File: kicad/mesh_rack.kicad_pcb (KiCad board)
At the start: 4 copper layers, 200 x 100 mm, 20 parts, among them IC1 E22-900M22S, J1 Input, U1 INA260, U2 ESP32-S3-WROOM-1, U3 LM22678TJ-5, U4 LM2596S-3.3, U5 TPD2EUSB30

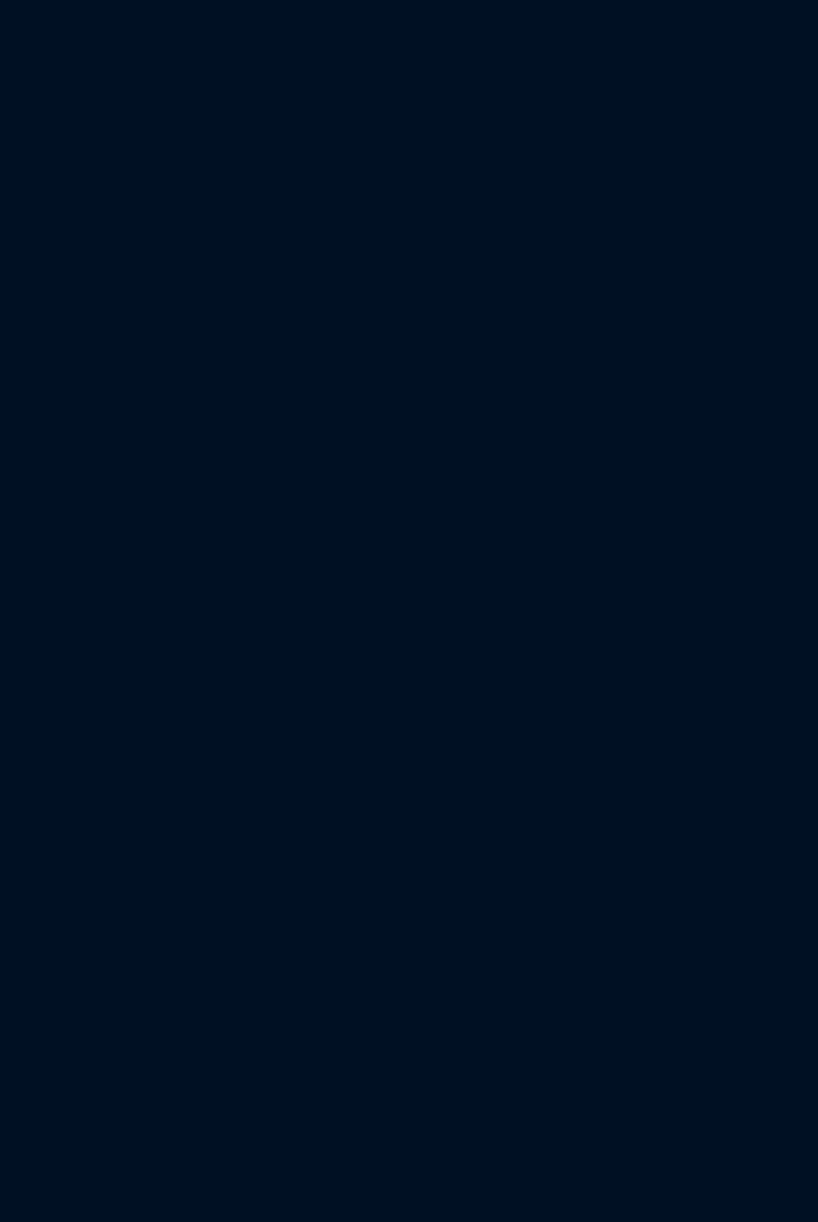
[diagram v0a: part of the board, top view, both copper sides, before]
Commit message: add expansin headers
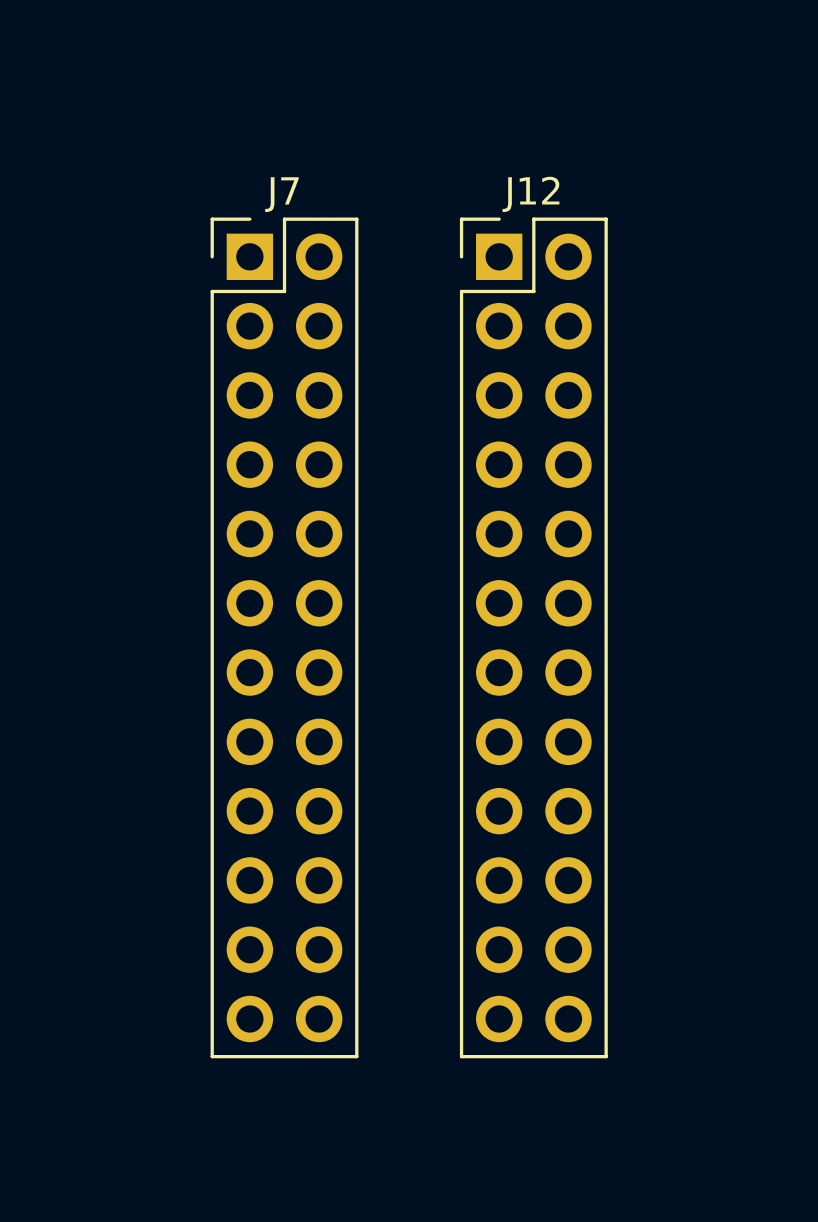
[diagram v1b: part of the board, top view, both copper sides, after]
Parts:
- added J12: Conn_02x12_Odd_Even, Connector_PinHeader_2.54mm:PinHeader_2x12_P2.54mm_Vertical, F.Cu at (250.7, 49.1)
- added J7: Conn_02x12_Odd_Even, Connector_PinHeader_2.54mm:PinHeader_2x12_P2.54mm_Vertical, F.Cu at (241.6, 49.1)

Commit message: finish pcb
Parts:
- removed J12: Conn_02x12_Odd_Even, Connector_PinHeader_2.54mm:PinHeader_2x12_P2.54mm_Vertical
- removed JP1: A0, Jumper:SolderJumper-2_P1.3mm_Open_TrianglePad1.0x1.5mm
- removed JP2: A1, Jumper:SolderJumper-2_P1.3mm_Open_TrianglePad1.0x1.5mm
- added C1: 10uF, Capacitor_SMD:C_0805_2012Metric, F.Cu at (114.2, 33.2)
- added C10: 47uF, Capacitor_SMD:C_0805_2012Metric, F.Cu at (71.2, 80.8)
- added C11: 100nF, Capacitor_SMD:C_0805_2012Metric, F.Cu at (59.0, 83.8)
- added C12: 100nF, Capacitor_SMD:C_0805_2012Metric, F.Cu at (69.2, 100.2)
- added C13: 0.1uF, Capacitor_SMD:C_0805_2012Metric, F.Cu at (99.5, 86.9)
- added C14: 470uF, Capacitor_SMD:C_0805_2012Metric, F.Cu at (76.8, 92.9)
- added C15: 10uF, Capacitor_SMD:C_0805_2012Metric, F.Cu at (78.8, 92.9)
- added C16: 0.1uF, Capacitor_SMD:C_0805_2012Metric, F.Cu at (80.8, 92.9)
- added C17: 470uF, Capacitor_SMD:C_0805_2012Metric, F.Cu at (82.8, 92.9)
- added C18: 22uF, Capacitor_SMD:C_0805_2012Metric, F.Cu at (99.5, 80.9)
- added C19: 680uF, Capacitor_SMD:C_0805_2012Metric, F.Cu at (99.5, 82.9)
- added C2: 0.1uF, Capacitor_SMD:C_0805_2012Metric, F.Cu at (112.2, 33.2)
- added C20: 680uF, Capacitor_SMD:C_0805_2012Metric, F.Cu at (99.5, 84.9)
- added C21: 0.1uF, Capacitor_SMD:C_0805_2012Metric, F.Cu at (74.8, 101.4)
- added C22: 100nF, Capacitor_SMD:C_0805_2012Metric, F.Cu at (189.1, 35.0)
- added C23: 10uF, Capacitor_SMD:C_0805_2012Metric, F.Cu at (189.1, 33.0)
- added C24: 0.1uF, Capacitor_SMD:C_0805_2012Metric, F.Cu at (111.5, 41.8)
- added C3: 1uF, Capacitor_SMD:C_0805_2012Metric, F.Cu at (106.2, 39.0)
- added C4: 0.1uF, Capacitor_SMD:C_0805_2012Metric, F.Cu at (155.6, 47.7)
- added C5: 22uF, Capacitor_SMD:C_0805_2012Metric, F.Cu at (45.8, 83.2)
- added C6: 22uF, Capacitor_SMD:C_0805_2012Metric, F.Cu at (48.8, 83.2)
- added C7: 100uF, Capacitor_SMD:C_0805_2012Metric, F.Cu at (51.8, 83.2)
- added C8: 47uF, Capacitor_SMD:C_0805_2012Metric, F.Cu at (71.2, 74.7)
- added C9: 220uF, Capacitor_SMD:C_0805_2012Metric, F.Cu at (71.2, 77.8)
- added D4: LED, LED_THT:LED_D5.0mm, F.Cu at (130.8, 60.0)
- added D5: LED, LED_THT:LED_D5.0mm, F.Cu at (48.2, 30.2)
- added D6: LED, LED_THT:LED_D5.0mm, F.Cu at (106.8, 91.2)
- added D7: LED, LED_THT:LED_D5.0mm, F.Cu at (77.8, 73.7)
- added D8: LED, LED_THT:LED_D5.0mm, F.Cu at (65.5, 110.2)
- added D9: LED, LED_THT:LED_D5.0mm, F.Cu at (124.2, 60.0)
- added J10: Conn_01x02, Connector_PinSocket_2.54mm:PinSocket_1x02_P2.54mm_Vertical, F.Cu at (41.0, 43.8)
- added J11: Conn_01x04, Connector_PinHeader_2.54mm:PinHeader_1x04_P2.54mm_Vertical, F.Cu at (99.0, 51.1)
- added J2: Power Switch, TerminalBlock_Altech:Altech_AK100_1x02_P5.00mm, F.Cu at (44.1, 95.0)
- added J3: USB_C_Receptacle_USB2.0_14P, Connector_USB:USB_C_Receptacle_HRO_TYPE-C-31-M-12, F.Cu at (82.5, 29.7)
- added J4: Conn_01x02, Connector_PinSocket_2.54mm:PinSocket_1x02_P2.54mm_Vertical, F.Cu at (61.0, 44.8)
- added J5: BOOT, Connector_PinHeader_2.54mm:PinHeader_1x02_P2.54mm_Vertical, F.Cu at (151.0, 46.5)
- added J6: EN, Connector_PinHeader_2.54mm:PinHeader_1x02_P2.54mm_Vertical, F.Cu at (105.2, 42.0)
- added J8: Conn_02x09_Counter_Clockwise, Connector_PinHeader_2.54mm:PinHeader_2x09_P2.54mm_Vertical, F.Cu at (178.4, 80.5)
- added J9: Conn_01x10, Connector_PinSocket_2.54mm:PinSocket_1x10_P2.54mm_Vertical, F.Cu at (146.5, 79.6)
- added L1: 10uH Coilcraft XAL7030-103, Inductor_SMD:L_Coilcraft_XAL7030-103, F.Cu at (64.8, 77.8)
- added L2: 22uH, Inductor_SMD:L_12x12mm_H4.5mm, F.Cu at (86.5, 83.9)
- added Q1: IRF9540N, Package_TO_SOT_THT:TO-220-3_Vertical, F.Cu at (44.2, 106.5)
- added Q2: IRF540N, Package_TO_SOT_THT:TO-220-3_Vertical, F.Cu at (53.5, 54.2)
- added R1: 10k, Resistor_THT:R_Axial_DIN0207_L6.3mm_D2.5mm_P10.16mm_Horizontal, F.Cu at (102.4, 36.5)
- added R10: 47k, Resistor_THT:R_Axial_DIN0207_L6.3mm_D2.5mm_P10.16mm_Horizontal, F.Cu at (74.7, 105.9)
- added R11: 47k, Resistor_THT:R_Axial_DIN0207_L6.3mm_D2.5mm_P10.16mm_Horizontal, F.Cu at (98.4, 105.9)
- added R12: 22, Resistor_SMD:R_0805_2012Metric_Pad1.20x1.40mm_HandSolder, F.Cu at (83.2, 39.2)
- added R13: 22, Resistor_SMD:R_0805_2012Metric_Pad1.20x1.40mm_HandSolder, F.Cu at (81.2, 39.2)
- added R14: 5.1k, Resistor_SMD:R_0805_2012Metric_Pad1.20x1.40mm_HandSolder, F.Cu at (77.8, 39.2)
- added R15: 5.1k, Resistor_SMD:R_0805_2012Metric_Pad1.20x1.40mm_HandSolder, F.Cu at (86.8, 39.2)
- added R16: 10k, Resistor_THT:R_Axial_DIN0207_L6.3mm_D2.5mm_P10.16mm_Horizontal, F.Cu at (150.4, 59.2)
- added R17: 10k, Resistor_THT:R_Axial_DIN0207_L6.3mm_D2.5mm_P10.16mm_Horizontal, F.Cu at (160.3, 77.0)
- added R18: 10k, Resistor_THT:R_Axial_DIN0207_L6.3mm_D2.5mm_P10.16mm_Horizontal, F.Cu at (150.6, 53.4)
- added R19: 10k, Resistor_THT:R_Axial_DIN0207_L6.3mm_D2.5mm_P10.16mm_Horizontal, F.Cu at (142.8, 53.8)
- added R2: 10k, Resistor_THT:R_Axial_DIN0207_L6.3mm_D2.5mm_P10.16mm_Horizontal, F.Cu at (68.0, 28.9)
- added R20: 10k, Resistor_THT:R_Axial_DIN0207_L6.3mm_D2.5mm_P10.16mm_Horizontal, F.Cu at (117.0, 64.1)
- added R21: 10k, Resistor_THT:R_Axial_DIN0207_L6.3mm_D2.5mm_P10.16mm_Horizontal, F.Cu at (71.0, 114.8)
- added R22: 10k, Resistor_THT:R_Axial_DIN0207_L6.3mm_D2.5mm_P10.16mm_Horizontal, F.Cu at (124.5, 64.2)
- added R3: 10k, Resistor_THT:R_Axial_DIN0207_L6.3mm_D2.5mm_P10.16mm_Horizontal, F.Cu at (130.8, 64.2)
- added R4: 10k, Resistor_THT:R_Axial_DIN0207_L6.3mm_D2.5mm_P10.16mm_Horizontal, F.Cu at (48.9, 108.8)
- added R5: 10k, Resistor_THT:R_Axial_DIN0207_L6.3mm_D2.5mm_P10.16mm_Horizontal, F.Cu at (51.7, 30.5)
- added R6: 10k, Resistor_THT:R_Axial_DIN0207_L6.3mm_D2.5mm_P10.16mm_Horizontal, F.Cu at (111.0, 91.4)
- added R7: 10k, Resistor_THT:R_Axial_DIN0207_L6.3mm_D2.5mm_P10.16mm_Horizontal, F.Cu at (81.4, 73.8)
- added R8: 100k, Resistor_THT:R_Axial_DIN0207_L6.3mm_D2.5mm_P10.16mm_Horizontal, F.Cu at (63.6, 103.2)
- added R9: 18k, Resistor_THT:R_Axial_DIN0207_L6.3mm_D2.5mm_P10.16mm_Horizontal, F.Cu at (53.4, 100.2)
- J7: value Conn_02x12_Odd_Even -> Conn_Coaxial_Small; footprint Connector_PinHeader_2.54mm:PinHeader_2x12_P2.54mm_Vertical -> Connector_Coaxial:U.FL_Molex_MCRF_73412-0110_Vertical
- U1: value INA260 -> NEO-M8N; footprint Package_SO:TSSOP-16_4.4x5mm_P0.65mm -> RF_GPS:ublox_NEO
- moved U1 225.7 mm to (51.0, 43.2)
- moved U5 211.8 mm to (82.2, 43.4)
- moved J1 204.9 mm to (48.8, 112.8)
- moved J7 203.3 mm to (38.2, 49.0), turned to 90 degrees
- moved D1 198.1 mm to (49.0, 104.2), turned to -90 degrees
- moved D2 187.0 mm to (76.3, 86.1), turned to 90 degrees
- moved U3 181.8 mm to (62.9, 91.5)
- moved D3 179.7 mm to (58.0, 115.2), turned to -90 degrees
- moved U4 152.6 mm to (95.2, 98.0)
- moved U2 148.7 mm to (125.1, 38.0)
- moved IC1 120.6 mm to (195.8, 45.0), turned to 90 degrees
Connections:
- IC1 pad 13: /ESP32/IO7 -> /ESP32/LORA_DIO1
- IC1 pad 14: /LoRa/IO0 -> /ESP32/LORA_BUSY
- IC1 pad 15: /LoRa/IO1 -> /ESP32/LORA_RST
- IC1 pad 16: /ESP32/IO10 -> /ESP32/LORA_MISO
- IC1 pad 17: /ESP32/IO11 -> /ESP32/LORA_MOSI
- IC1 pad 18: /ESP32/IO18 -> /ESP32/LORA_SCK
- IC1 pad 19: /ESP32/IO16 -> /ESP32/LORA_NSS
- IC1 pad 6: /LoRa/IO2 -> /ESP32/LORA_RF_SW
- IC1 pad 7: /ESP32/IO9 -> Net-(IC1-DIO2)
- IC1 pad 8: /ESP32/IO8 -> Net-(IC1-DIO2)
- J7 pad 1: Net-(J7-Pin_1) -> Net-(J7-In)
- J7 pad 2: Net-(J7-Pin_1) -> GND
- U1 pad 1: Net-(J2-Pin_2) -> unconnected-(U1-~{SAFEBOOT}-Pad1)
- U1 pad 10: +3.3V -> Net-(Q2-D)
- U1 pad 11: GND -> Net-(J7-In)
- U1 pad 12: Net-(J2-Pin_2) -> Net-(Q2-D)
- U1 pad 13: unconnected-(U1-NC-Pad13) -> Net-(Q2-D)
- U1 pad 14: /Power Input/RAW -> unconnected-(U1-LNA_EN-Pad14)
- U1 pad 15: /Power Input/RAW -> unconnected-(U1-RESERVED-Pad15)
- U1 pad 16: /Power Input/RAW -> unconnected-(U1-RESERVED-Pad16)
- U1 pad 2: Net-(J2-Pin_2) -> unconnected-(U1-D_SEL-Pad2)
- U1 pad 3: Net-(J2-Pin_2) -> /GPS/TIMEPULSE
- U1 pad 4: Net-(JP2-B) -> unconnected-(U1-EXTINT-Pad4)
- U1 pad 5: Net-(JP1-B) -> /GPS/GPS_USB_D-
- U1 pad 6: GND -> /GPS/GPS_USB_D+
- U1 pad 7: /ESP32/IO4 -> GND
- U1 pad 8: /ESP32/IO5 -> /ESP32/IO47
- U1 pad 9: /ESP32/IO6 -> unconnected-(U1-VCC_RF-Pad9)
- U2 pad 10: /ESP32/IO17 -> /ESP32/OLED_SDA
- U2 pad 11: /ESP32/IO18 -> /ESP32/OLED_SCL
- U2 pad 12: /ESP32/IO8 -> /ESP32/LORA_SCK
- U2 pad 17: /ESP32/IO9 -> /ESP32/LORA_MISO
- U2 pad 18: /ESP32/IO10 -> /ESP32/LORA_MOSI
- U2 pad 23: /ESP32/IO21 -> /ESP32/TST_PD0
- U2 pad 25: /ESP32/IO48 -> /ESP32/LED
- U2 pad 31: /ESP32/IO38 -> /ESP32/LORA_RF_SW
- U2 pad 32: /ESP32/IO39 -> /ESP32/LORA_DIO1
- U2 pad 33: /ESP32/IO40 -> /ESP32/LORA_BUSY
- U2 pad 34: /ESP32/IO41 -> /ESP32/LORA_NSS
- U2 pad 35: /ESP32/IO42 -> /ESP32/LORA_RST
- U2 pad 36: /ESP32/RXD0 -> /ESP32/MCU_RXD0
- U2 pad 37: /ESP32/TXD0 -> /ESP32/MCU_TXD0
- U2 pad 39: /ESP32/IO1 -> /ESP32/ADC1
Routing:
- net +5V: track 0.00 -> 196.8 mm
- net +3.3V: track 0.00 -> 172.6 mm, vias 0 -> 1
- net GND: track 0.00 -> 150.7 mm, vias 0 -> 356
- net /ESP32/IO47: track 0.00 -> 114.0 mm, vias 0 -> 1
- net /ESP32/IO16: track 0.00 -> 110.0 mm, vias 0 -> 2
- net /ESP32/IO45: track 0.00 -> 109.6 mm
- net /ESP32/IO5: track 0.00 -> 100.7 mm, vias 0 -> 1
- net /ESP32/IO7: track 0.00 -> 99.5 mm, vias 0 -> 1
- net /ESP32/LORA_SCK: track 0.00 -> 90.7 mm, vias 0 -> 2
- net /ESP32/IO11: track 0.00 -> 90.1 mm, vias 0 -> 1
- net /ESP32/IO6: track 0.00 -> 88.8 mm, vias 0 -> 1
- net /ESP32/LORA_MISO: track 0.00 -> 86.7 mm, vias 0 -> 2
- net /ESP32/IO46: track 0.00 -> 85.9 mm
- net /ESP32/MCU_RXD0: track 0.00 -> 83.0 mm, vias 0 -> 2
- net /ESP32/MCU_TXD0: track 0.00 -> 82.8 mm, vias 0 -> 2
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- added copper zone on In2.Cu, net +3.3V
- added copper zone on F.Cu, net +5V
- added copper zone on F.Cu, net GND
- added copper zone on F.Cu, net Net-(Q2-D)
- added copper zone on F.Cu, net Net-(U3-SW)
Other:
- board text added: "ADC1 IO3 IO5 IO7 IO16 5V 3.3V 3.3V GND"
- board text added: "BOOT"
- board text added: "D+"
- board text added: "D-"
- board text added: "DAT2 DAT3 CD CMD VDD CLK VSS DAT0 DAT1 DET SHIELD"
- board text added: "EN"
- board text added: "IO2 IO4 IO6 IO11 IO46 5V 3.3V GND GND"
- board text added: "SCL"
- board text added: "SDA"
- board text added: "SDA SCL 3.3V GND"

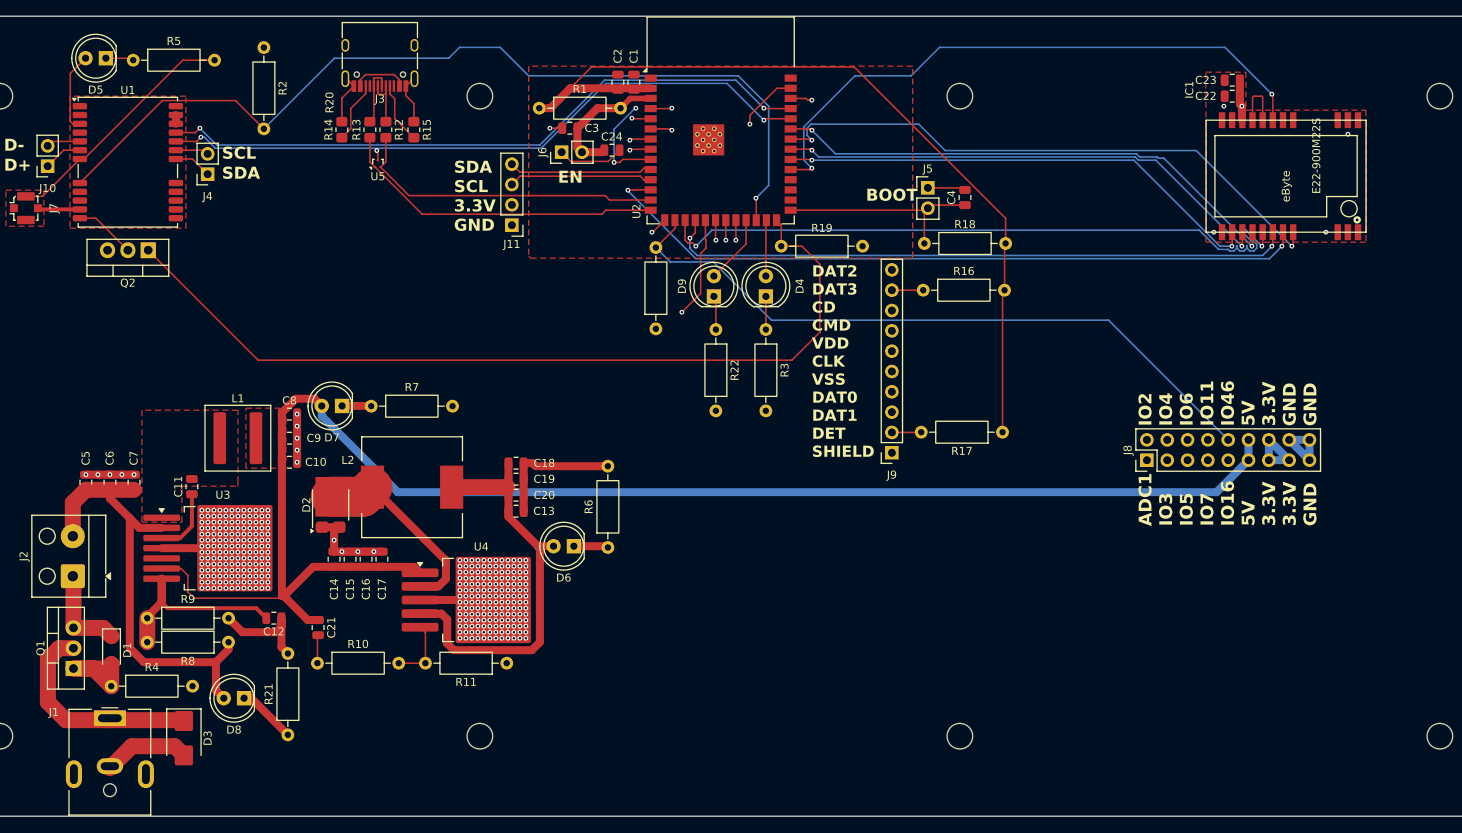
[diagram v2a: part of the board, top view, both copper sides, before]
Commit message: add current sensor
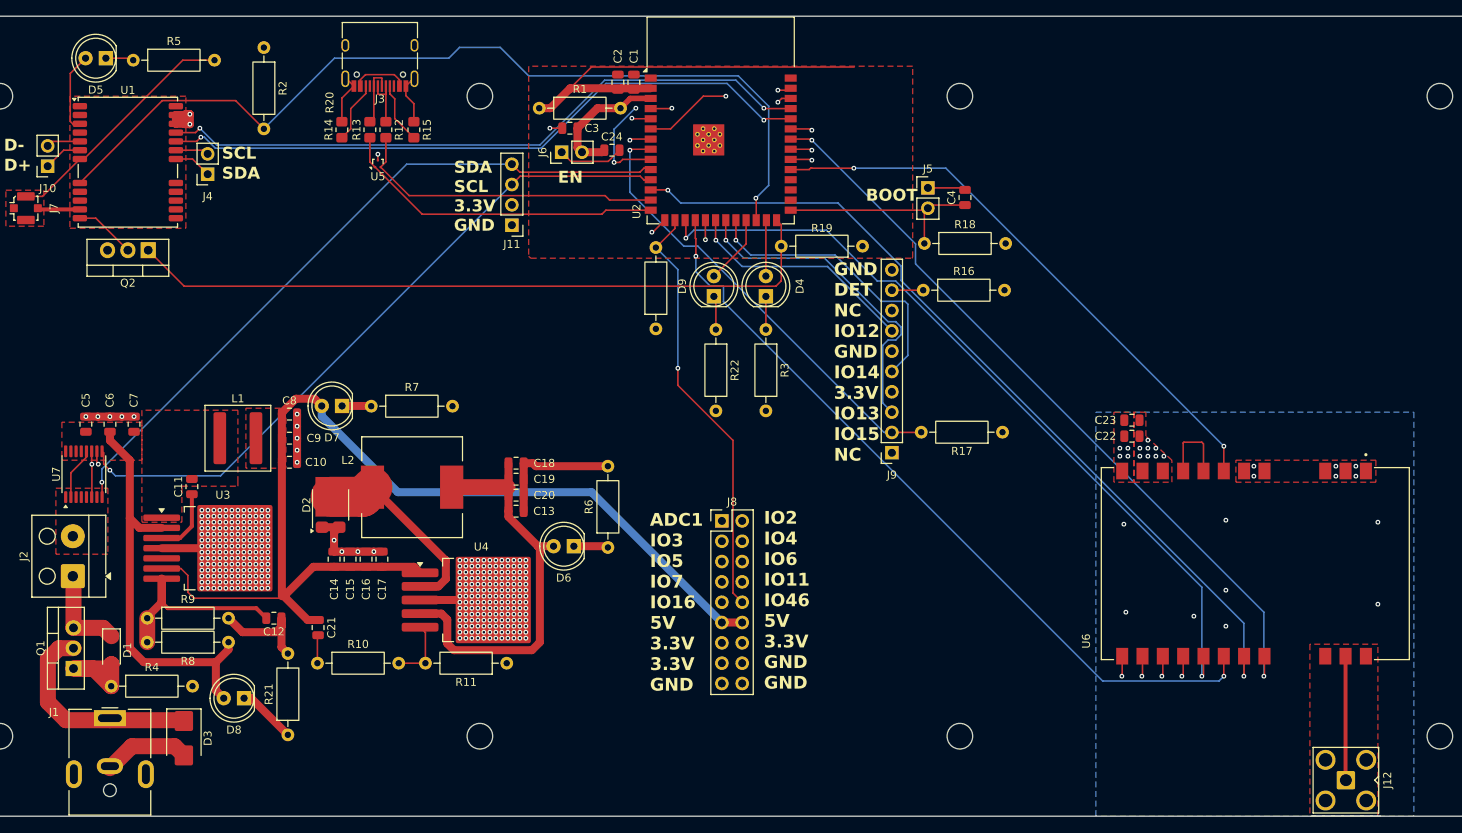
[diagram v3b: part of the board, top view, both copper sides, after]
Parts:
- removed IC1: E22-900M22S, E22-900M22S:E22-900M22S
- added J12: Conn_Coaxial_Small, Connector_Coaxial:SMA_Amphenol_901-143_Horizontal, F.Cu at (203.2, 120.5)
- added U6: E22-900M30S, E22-900M30S:XCVR_E22-900M30S, F.Cu at (191.9, 93.4)
- added U7: INA260, Package_SO:TSSOP-16_4.4x5mm_P0.65mm, F.Cu at (45.5, 82.2)
- moved J8 53.7 mm to (125.2, 88.1), turned to 0 degrees
- moved C22 44.3 mm to (176.5, 77.5)
- moved C23 44.3 mm to (176.5, 75.5)
- moved C5 7.25 mm to (45.8, 76.0)
- moved C6 7.25 mm to (48.8, 76.0)
- moved C7 7.25 mm to (51.8, 76.0)
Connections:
- net /ESP32/OLED_SCL renamed SCL
- net /ESP32/OLED_SDA renamed SDA
- J2 pad 2: /Power Input/RAW -> Net-(J2-Pin_2)
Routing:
- net SDA: track 18.0 -> 88.6 mm, vias 0 -> 1
- net SCL: track 18.0 -> 86.4 mm, vias 0 -> 1
- net +5V: track 196.8 -> 136.0 mm
- net +3.3V: track 172.6 -> 116.7 mm, vias 1 -> 11
- net /ESP32/IO5: track 100.7 -> 62.5 mm
- net /ESP32/IO3: track 81.3 -> 44.6 mm
- net /ESP32/IO7: track 99.5 -> 63.3 mm
- net /ESP32/IO16: track 110.0 -> 75.6 mm
- net /ESP32/IO46: track 85.9 -> 53.2 mm, vias 0 -> 1
- net /ESP32/LORA_RST: track 65.5 -> 92.7 mm
- net /ESP32/LORA_BUSY: track 63.2 -> 89.1 mm
- net /ESP32/LORA_DIO1: track 61.4 -> 87.2 mm
- net /ESP32/LORA_NSS: track 73.4 -> 95.6 mm
- net /ESP32/IO45: track 109.6 -> 89.9 mm
- net /ESP32/LORA_MOSI: track 79.2 -> 97.6 mm
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- added copper zone on F.Cu, net +3.3V
- added copper zone on F.Cu, net /Power Input/RAW
- added copper zone on B.Cu, net GND
- added copper zone on F.Cu, net Net-(J2-Pin_2)
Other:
- board text added: "GND DET NC IO12 GND IO14 3.3V IO13 IO15 NC"
- board text removed: "DAT2 DAT3 CD CMD VDD CLK VSS DAT0 DAT1 DET SHIELD"
